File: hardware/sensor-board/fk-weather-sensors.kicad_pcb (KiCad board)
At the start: 2 copper layers, 14.2 x 21.6 mm, 10 parts, among them J1 CONN_01X06, U1 MPL3115A2, U2 TSL2591, U3 SHT31

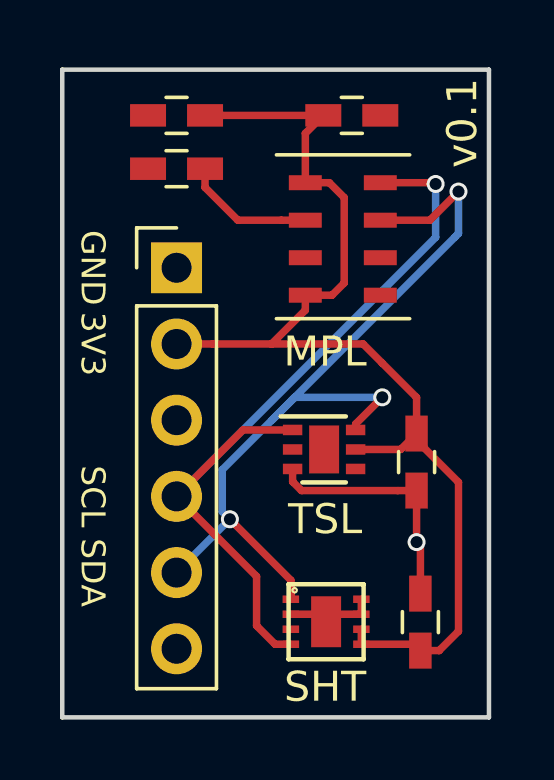
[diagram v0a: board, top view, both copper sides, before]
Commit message: Change header orien. Plot.
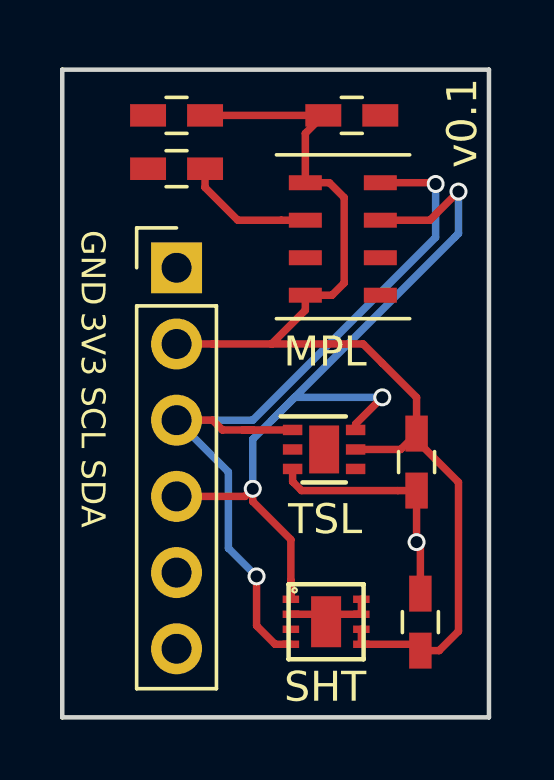
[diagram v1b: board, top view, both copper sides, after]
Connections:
- net 5V0 renamed Net-(J1-Pad6)
- J1 pad 3: Net-(J1-Pad3) -> /SCL
- J1 pad 4: /SCL -> /SDA
- J1 pad 5: /SDA -> Net-(J1-Pad5)
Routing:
- net /SCL: track 27.5 -> 28.5 mm, vias 1 -> 2
- net /SDA: track 29.3 -> 28.6 mm

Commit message: Change version to 0.6.
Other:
- board text added: "v0.6"
- board text removed: "v0.1"
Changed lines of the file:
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@@
     (arrow2b (pts (xy 140.716 101.854) (xy 141.842504 101.267579)))
   )
-  (gr_text v0.1 (at 154.051 105.918 90) (layer F.SilkS)
+  (gr_text v0.6 (at 154.051 105.918 90) (layer F.SilkS)
     (effects (font (size 1 1) (thickness 0.15)))
   )
